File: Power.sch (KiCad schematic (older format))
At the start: 17 parts, among them CON1 PWR_JACK, P1 PWR_USB, U1 MCP16312-E/MS

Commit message: Schematic changes. PCB in process of making.
Removed LAN9500A Jtag. Removed Aria G25 pinout. Removed USB connectors. Added rezistors to USB/ETH/ySD shields.
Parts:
- removed P1: PWR_USB, symbol USB_OTG
- CON1: footprint (none) -> Connectors:BARREL_JACK
- D1, D2: footprint (none) -> Diodes_SMD:D_SMA_Handsoldering
- L1: footprint (none) -> Choke_SMD:Choke_SMD_1206_Handsoldering
- U1: footprint (none) -> Housings_SSOP:MSOP-8-1EP_3x3mm_Pitch0.65mm
- W1: footprint (none) -> Measurement_Points:Measurement_Point_Square-SMD-Pad_Small
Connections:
- net VBUS: now reaches D1.2 (A)
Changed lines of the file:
@@
 F 0 "CON1" H 3600 2850 50  0000 C CNN
 F 1 "PWR_JACK" H 3600 2400 50  0000 C CNN
-F 2 "" H 3600 2600 50  0001 C CNN
+F 2 "Connectors:BARREL_JACK" H 3600 2600 50  0001 C CNN
 F 3 "" H 3600 2600 50  0000 C CNN
 	1    3600 2600
 	1    0    0    -1
-$EndComp
-$Comp
-L USB_OTG P1
-U 1 1 587BE3DA
-P 4250 3700
-F 0 "P1" V 4575 3575 50  0000 C CNN
-F 1 "PWR_USB" V 3950 3700 50  0000 C CNN
-F 2 "" V 4200 3600 50  0001 C CNN
-F 3 "" V 4200 3600 50  0000 C CNN
-	1    4250 3700
-	0    1    1    0
 $EndComp
 $Comp
@@
 $EndComp
 $Comp
-L GND #PWR02
-U 1 1 587BE697
-P 4350 4200
-F 0 "#PWR02" H 4350 3950 50  0001 C CNN
-F 1 "GND" H 4350 4050 50  0000 C CNN
-F 2 "" H 4350 4200 50  0000 C CNN
-F 3 "" H 4350 4200 50  0000 C CNN
-	1    4350 4200
-	1    0    0    -1
-$EndComp
-$Comp
-L GND #PWR03
-U 1 1 587BE6AA
-P 3850 4000
-F 0 "#PWR03" H 3850 3750 50  0001 C CNN
-F 1 "GND" H 3850 3850 50  0000 C CNN
-F 2 "" H 3850 4000 50  0000 C CNN
-F 3 "" H 3850 4000 50  0000 C CNN
-	1    3850 4000
-	1    0    0    -1
-$EndComp
-$Comp
-L PWR_FLAG #FLG04
+L PWR_FLAG #FLG02
 U 1 1 587BE76C
 P 8150 2500
-F 0 "#FLG04" H 8150 2595 50  0001 C CNN
+F 0 "#FLG02" H 8150 2595 50  0001 C CNN
 F 1 "PWR_FLAG" H 8050 2700 50  0000 C CNN
 F 2 "" H 8150 2500 50  0000 C CNN
@@
 F 0 "D2" H 4250 2400 50  0000 C CNN
 F 1 "Schottky" H 4300 2600 50  0000 C CNN
-F 2 "" H 4250 2500 50  0001 C CNN
+F 2 "Diodes_SMD:D_SMA_Handsoldering" H 4250 2500 50  0001 C CNN
 F 3 "" H 4250 2500 50  0000 C CNN
 	1    4250 2500
@@
 F 0 "U1" H 6550 2400 50  0000 C CNN
 F 1 "MCP16312-E/MS" H 6550 2950 50  0000 C CNN
-F 2 "" H 6600 2900 60  0001 C CNN
+F 2 "Housings_SSOP:MSOP-8-1EP_3x3mm_Pitch0.65mm" H 6600 2900 60  0001 C CNN
 F 3 "" H 6600 2900 60  0001 C CNN
 	1    6500 2650
@@
 $EndComp
 $Comp
-L GND #PWR05
+L GND #PWR03
 U 1 1 587BECE9
 P 5950 2900
-F 0 "#PWR05" H 5950 2650 50  0001 C CNN
+F 0 "#PWR03" H 5950 2650 50  0001 C CNN
 F 1 "GND" H 5950 2750 50  0000 C CNN
 F 2 "" H 5950 2900 50  0000 C CNN
@@
 $EndComp
 $Comp
-L GND #PWR06
+L GND #PWR04
 U 1 1 587BED67
 P 5750 3200
-F 0 "#PWR06" H 5750 2950 50  0001 C CNN
+F 0 "#PWR04" H 5750 2950 50  0001 C CNN
 F 1 "GND" H 5750 3050 50  0000 C CNN
 F 2 "" H 5750 3200 50  0000 C CNN
@@
 $EndComp
 $Comp
-L GND #PWR07
+L GND #PWR05
 U 1 1 587BEE32
 P 5550 3000
-F 0 "#PWR07" H 5550 2750 50  0001 C CNN
+F 0 "#PWR05" H 5550 2750 50  0001 C CNN
 F 1 "GND" H 5550 2850 50  0000 C CNN
 F 2 "" H 5550 3000 50  0000 C CNN
@@
 $EndComp
 $Comp
-L GND #PWR08
+L GND #PWR06
 U 1 1 587BEE52
 P 5300 3000
-F 0 "#PWR08" H 5300 2750 50  0001 C CNN
+F 0 "#PWR06" H 5300 2750 50  0001 C CNN
 F 1 "GND" H 5300 2850 50  0000 C CNN
 F 2 "" H 5300 3000 50  0000 C CNN
@@
 VIN
 $Comp
-L GND #PWR09
+L GND #PWR07
 U 1 1 587BF3B1
 P 7100 2900
-F 0 "#PWR09" H 7100 2650 50  0001 C CNN
+F 0 "#PWR07" H 7100 2650 50  0001 C CNN
 F 1 "GND" H 7100 2750 50  0000 C CNN
 F 2 "" H 7100 2900 50  0000 C CNN
@@
 F 0 "L1" V 7600 2700 50  0000 C CNN
 F 1 "15uH" V 7750 2600 50  0000 C CNN
-F 2 "" H 7650 2600 50  0001 C CNN
+F 2 "Choke_SMD:Choke_SMD_1206_Handsoldering" H 7650 2600 50  0001 C CNN
 F 3 "" H 7650 2600 50  0000 C CNN
 	1    7650 2600
@@
 $EndComp
 $Comp
-L GND #PWR010
+L GND #PWR08
 U 1 1 587BF576
 P 7900 3500
-F 0 "#PWR010" H 7900 3250 50  0001 C CNN
+F 0 "#PWR08" H 7900 3250 50  0001 C CNN
 F 1 "GND" H 7900 3350 50  0000 C CNN
 F 2 "" H 7900 3500 50  0000 C CNN
@@
 $EndComp
 $Comp
-L GND #PWR011
+L GND #PWR09
 U 1 1 587BFB09
 P 8150 3100
-F 0 "#PWR011" H 8150 2850 50  0001 C CNN
+F 0 "#PWR09" H 8150 2850 50  0001 C CNN
 F 1 "GND" H 8150 2950 50  0000 C CNN
 F 2 "" H 8150 3100 50  0000 C CNN
@@
 $EndComp
 $Comp
-L GND #PWR012
+L GND #PWR010
 U 1 1 587BFB3B
 P 8400 3100
-F 0 "#PWR012" H 8400 2850 50  0001 C CNN
+F 0 "#PWR010" H 8400 2850 50  0001 C CNN
 F 1 "GND" H 8400 2950 50  0000 C CNN
 F 2 "" H 8400 3100 50  0000 C CNN
@@
 $EndComp
 $Comp
-L +3.3V #PWR013
+L +3.3V #PWR011
 U 1 1 587C072D
 P 8400 2500
-F 0 "#PWR013" H 8400 2350 50  0001 C CNN
+F 0 "#PWR011" H 8400 2350 50  0001 C CNN
 F 1 "+3.3V" H 8400 2640 50  0000 C CNN
 F 2 "" H 8400 2500 50  0000 C CNN
@@
 Wire Wire Line
 	3950 3500 3850 3500
-Wire Wire Line
-	3850 3900 3850 4000
-Wire Wire Line
-	3850 3900 3950 3900
-Wire Wire Line
-	4350 4200 4350 4100
 Wire Wire Line
 	4000 2600 4000 2800
@@
 F 0 "D1" H 3700 3600 50  0000 C CNN
 F 1 "Schottky" H 3700 3400 50  0000 C CNN
-F 2 "" H 3700 3500 50  0001 C CNN
+F 2 "Diodes_SMD:D_SMA_Handsoldering" H 3700 3500 50  0001 C CNN
 F 3 "" H 3700 3500 50  0000 C CNN
 	1    3700 3500
@@
 $EndComp
 $Comp
-L GND #PWR014
+L GND #PWR012
 U 1 1 58981582
 P 8750 3500
-F 0 "#PWR014" H 8750 3250 50  0001 C CNN
+F 0 "#PWR012" H 8750 3250 50  0001 C CNN
 F 1 "GND" H 8750 3350 50  0000 C CNN
 F 2 "" H 8750 3500 50  0000 C CNN
@@
 F 0 "W1" H 8750 2770 50  0000 C CNN
 F 1 "3.3V_T" H 8750 2700 50  0000 C CNN
-F 2 "" H 8950 2500 50  0001 C CNN
+F 2 "Measurement_Points:Measurement_Point_Square-SMD-Pad_Small" H 8950 2500 50  0001 C CNN
 F 3 "" H 8950 2500 50  0000 C CNN
 	1    8750 2500
@@
 $EndComp
 Connection ~ 8750 2600
+Text HLabel 3950 3500 2    50   Input ~ 0
+VBUS
 $EndSCHEMATC

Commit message: Modified USB/ETH label names.
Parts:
- R1, R2, R3: footprint Resistors_SMD:R_0805_HandSoldering -> Resistors_SMD:R_0603_HandSoldering
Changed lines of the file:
@@
 F 0 "R1" V 7980 2850 50  0000 C CNN
 F 1 "31k6" V 7800 2850 50  0000 C CNN
-F 2 "Resistors_SMD:R_0805_HandSoldering" V 7830 2850 50  0001 C CNN
+F 2 "Resistors_SMD:R_0603_HandSoldering" V 7830 2850 50  0001 C CNN
 F 3 "" H 7900 2850 50  0000 C CNN
 	1    7900 2850
@@
 F 0 "R2" V 7980 3250 50  0000 C CNN
 F 1 "10k" V 7800 3250 50  0000 C CNN
-F 2 "Resistors_SMD:R_0805_HandSoldering" V 7830 3250 50  0001 C CNN
+F 2 "Resistors_SMD:R_0603_HandSoldering" V 7830 3250 50  0001 C CNN
 F 3 "" H 7900 3250 50  0000 C CNN
 	1    7900 3250
@@
 F 0 "R3" V 8830 3250 50  0000 C CNN
 F 1 "R" V 8750 3250 50  0000 C CNN
-F 2 "Resistors_SMD:R_0805_HandSoldering" V 8680 3250 50  0001 C CNN
+F 2 "Resistors_SMD:R_0603_HandSoldering" V 8680 3250 50  0001 C CNN
 F 3 "" H 8750 3250 50  0000 C CNN
 	1    8750 3250

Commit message: Finished first version of PCB.
Modified RJ45 footprint.
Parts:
- C1, C2: footprint Capacitors_SMD:C_0805_HandSoldering -> Capacitors_SMD:CP_Elec_5x4.5
- R3: value R -> 220
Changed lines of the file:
@@
 F 0 "C1" H 5200 2850 50  0000 L CNN
 F 1 "10uF" H 5100 2650 50  0000 L CNN
-F 2 "Capacitors_SMD:C_0805_HandSoldering" H 5338 2600 50  0001 C CNN
+F 2 "Capacitors_SMD:CP_Elec_5x4.5" H 5338 2600 50  0001 C CNN
 F 3 "" H 5300 2750 50  0000 C CNN
 	1    5300 2750
@@
 F 0 "C2" H 5450 2850 50  0000 L CNN
 F 1 "10uF" H 5350 2650 50  0000 L CNN
-F 2 "Capacitors_SMD:C_0805_HandSoldering" H 5588 2600 50  0001 C CNN
+F 2 "Capacitors_SMD:CP_Elec_5x4.5" H 5588 2600 50  0001 C CNN
 F 3 "" H 5550 2750 50  0000 C CNN
 	1    5550 2750
@@
 P 8750 3250
 F 0 "R3" V 8830 3250 50  0000 C CNN
-F 1 "R" V 8750 3250 50  0000 C CNN
+F 1 "220" V 8750 3250 50  0000 C CNN
 F 2 "Resistors_SMD:R_0603_HandSoldering" V 8680 3250 50  0001 C CNN
 F 3 "" H 8750 3250 50  0000 C CNN

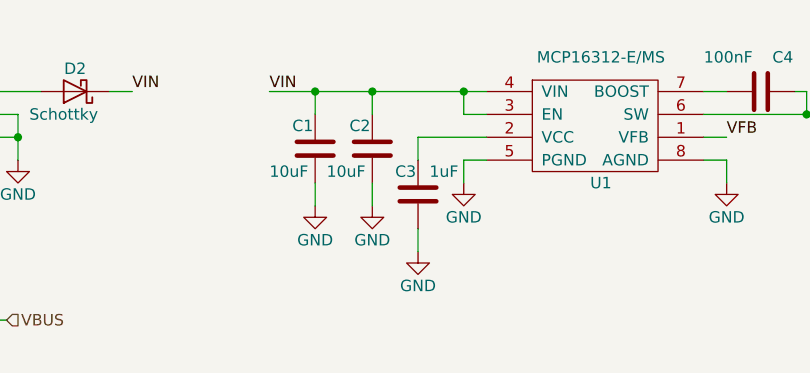
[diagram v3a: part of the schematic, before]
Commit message: Modified buck circuit on board.
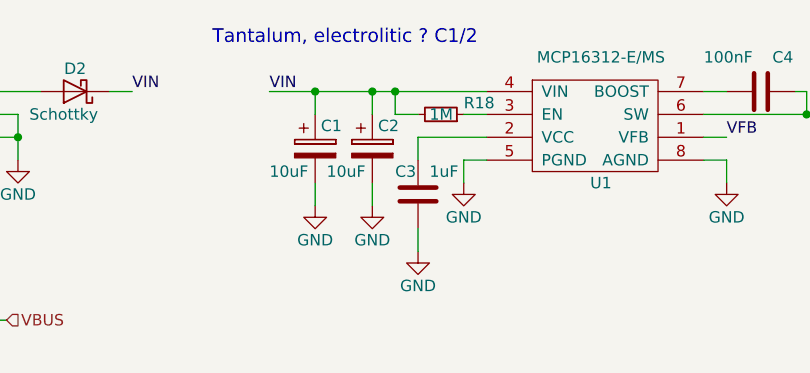
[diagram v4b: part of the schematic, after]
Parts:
- removed C1, C2: 10uF, Capacitors_SMD:CP_Elec_5x4.5, symbol C
- added C1, C2: 10uF, Capacitors_SMD:C_0603_HandSoldering, symbol CP
- added R18: 1M, Resistors_SMD:R_0603_HandSoldering, symbol R_Small
- C3, C4, C5, C6: footprint Capacitors_SMD:C_0805_HandSoldering -> Capacitors_SMD:C_0603_HandSoldering
- D3: footprint LEDs:LED_0805 -> LEDs:LED_0603
- L1: footprint Choke_SMD:Choke_SMD_1206_Handsoldering -> Inductors:Inductor_Taiyo-Yuden_MD-5050
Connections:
- net GND: now also C1.2, C2.2
- net VIN: now also C1.1, C2.1, R18.2; no longer U1.3 (EN)
- new net: R18.1, U1.3 (EN)
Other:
- note added: "Tantalum, electrolitic ? C1/2"
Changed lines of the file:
@@
 F 0 "C3" H 5650 3050 50  0000 L CNN
 F 1 "1uF" H 5800 3050 50  0000 L CNN
-F 2 "Capacitors_SMD:C_0805_HandSoldering" H 5788 2800 50  0001 C CNN
+F 2 "Capacitors_SMD:C_0603_HandSoldering" H 5788 2800 50  0001 C CNN
 F 3 "" H 5750 2950 50  0000 C CNN
 	1    5750 2950
-	1    0    0    -1
-$EndComp
-$Comp
-L C C1
-U 1 1 587BEC9F
-P 5300 2750
-F 0 "C1" H 5200 2850 50  0000 L CNN
-F 1 "10uF" H 5100 2650 50  0000 L CNN
-F 2 "Capacitors_SMD:CP_Elec_5x4.5" H 5338 2600 50  0001 C CNN
-F 3 "" H 5300 2750 50  0000 C CNN
-	1    5300 2750
 	1    0    0    -1
 $EndComp
@@
 $EndComp
 $Comp
-L C C2
-U 1 1 587BEDBB
-P 5550 2750
-F 0 "C2" H 5450 2850 50  0000 L CNN
-F 1 "10uF" H 5350 2650 50  0000 L CNN
-F 2 "Capacitors_SMD:CP_Elec_5x4.5" H 5588 2600 50  0001 C CNN
-F 3 "" H 5550 2750 50  0000 C CNN
-	1    5550 2750
-	1    0    0    -1
-$EndComp
-$Comp
 L GND #PWR05
 U 1 1 587BEE32
@@
 F 0 "L1" V 7600 2700 50  0000 C CNN
 F 1 "15uH" V 7750 2600 50  0000 C CNN
-F 2 "Choke_SMD:Choke_SMD_1206_Handsoldering" H 7650 2600 50  0001 C CNN
+F 2 "Inductors:Inductor_Taiyo-Yuden_MD-5050" H 7650 2600 50  0001 C CNN
 F 3 "" H 7650 2600 50  0000 C CNN
 	1    7650 2600
@@
 F 0 "C4" V 7100 2550 50  0000 L CNN
 F 1 "100nF" V 7100 2250 50  0000 L CNN
-F 2 "Capacitors_SMD:C_0805_HandSoldering" H 7288 2350 50  0001 C CNN
+F 2 "Capacitors_SMD:C_0603_HandSoldering" H 7288 2350 50  0001 C CNN
 F 3 "" H 7250 2500 50  0000 C CNN
 	1    7250 2500
@@
 F 0 "C5" H 8175 2950 50  0000 L CNN
 F 1 "10uF" H 8175 2750 50  0000 L CNN
-F 2 "Capacitors_SMD:C_0805_HandSoldering" H 8188 2700 50  0001 C CNN
+F 2 "Capacitors_SMD:C_0603_HandSoldering" H 8188 2700 50  0001 C CNN
 F 3 "" H 8150 2850 50  0000 C CNN
 	1    8150 2850
@@
 F 0 "C6" H 8425 2950 50  0000 L CNN
 F 1 "10uF" H 8425 2750 50  0000 L CNN
-F 2 "Capacitors_SMD:C_0805_HandSoldering" H 8438 2700 50  0001 C CNN
+F 2 "Capacitors_SMD:C_0603_HandSoldering" H 8438 2700 50  0001 C CNN
 F 3 "" H 8400 2850 50  0000 C CNN
 	1    8400 2850
@@
 	6050 2600 5950 2600
 Wire Wire Line
-	5950 2600 5950 2500
-Wire Wire Line
-	5100 2500 6050 2500
-Wire Wire Line
 	5950 2900 5950 2800
 Wire Wire Line
@@
 Wire Wire Line
 	5550 2500 5550 2600
-Connection ~ 5950 2500
 Wire Wire Line
 	5300 2500 5300 2600
@@
 F 0 "D3" H 8750 2950 50  0000 C CNN
 F 1 "PWR_LED" H 8750 2750 50  0000 C CNN
-F 2 "LEDs:LED_0805" H 8750 2850 50  0001 C CNN
+F 2 "LEDs:LED_0603" H 8750 2850 50  0001 C CNN
 F 3 "" H 8750 2850 50  0000 C CNN
 	1    8750 2850
@@
 Text HLabel 3950 3500 2    50   Input ~ 0
 VBUS
+$Comp
+L CP C1
+U 1 1 58B7F09F
+P 5300 2750
+F 0 "C1" H 5325 2850 50  0000 L CNN
+F 1 "10uF" H 5100 2650 50  0000 L CNN
+F 2 "Capacitors_SMD:C_0603_HandSoldering" H 5338 2600 50  0001 C CNN
+F 3 "" H 5300 2750 50  0000 C CNN
+	1    5300 2750
+	1    0    0    -1
+$EndComp
+$Comp
+L CP C2
+U 1 1 58B7F361
+P 5550 2750
+F 0 "C2" H 5575 2850 50  0000 L CNN
+F 1 "10uF" H 5350 2650 50  0000 L CNN
+F 2 "Capacitors_SMD:C_0603_HandSoldering" H 5588 2600 50  0001 C CNN
+F 3 "" H 5550 2750 50  0000 C CNN
+	1    5550 2750
+	1    0    0    -1
+$EndComp
+Text Notes 4850 2300 0    60   ~ 0
+Tantalum, electrolitic ? C1/2
+$Comp
+L R_Small R18
+U 1 1 58B7E269
+P 5850 2600
+F 0 "R18" V 5900 2700 50  0000 L CNN
+F 1 "1M" V 5850 2550 50  0000 L CNN
+F 2 "Resistors_SMD:R_0603_HandSoldering" H 5850 2600 50  0001 C CNN
+F 3 "" H 5850 2600 50  0000 C CNN
+	1    5850 2600
+	0    1    -1   0
+$EndComp
+Wire Wire Line
+	5750 2600 5650 2600
+Wire Wire Line
+	5650 2600 5650 2500
+Connection ~ 5650 2500
+Wire Wire Line
+	5100 2500 6050 2500
 $EndSCHEMATC

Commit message: Modified schematic. v1.1
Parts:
- added C1, C2, C4, C6: 10uF, Capacitors_Tantalum_SMD:CP_Tantalum_Case-C_EIA-6032-28_Hand, symbol CP
- added C10: 100nF, Capacitors_SMD:C_0603_HandSoldering, symbol C
- added C12, C14: 10uF, Capacitors_SMD:C_0603_HandSoldering, symbol C
- added C8: 1uF, Capacitors_SMD:C_0603_HandSoldering, symbol C
- added D4: PWR_LED, LEDs:LED_0603, symbol LED
- added L2: 22uH, Inductors:Inductor_Taiyo-Yuden_MD-5050, symbol L
- added R2: 1M, Resistors_SMD:R_0603_HandSoldering, symbol R_Small
- added R5: 52k3, Resistors_SMD:R_0603_HandSoldering, symbol R
- added R6: 10k, Resistors_SMD:R_0603_HandSoldering, symbol R
- added R8: 220, Resistors_SMD:R_0603_HandSoldering, symbol R
- added U2: MCP16312-E/MS, Housings_SSOP:MSOP-8_3x3mm_Pitch0.65mm, symbol MCP16312-E/MS
- added W1: VBUS_T, Measurement_Points:Measurement_Point_Round-SMD-Pad_Small, symbol TEST_1P
- added W2: VIN_T, Measurement_Points:Measurement_Point_Round-SMD-Pad_Small, symbol TEST_1P
- added W4: 5V_T, Measurement_Points:Measurement_Point_Round-SMD-Pad_Small, symbol TEST_1P
- C3: renamed from C1; footprint Capacitors_SMD:C_0603_HandSoldering -> Capacitors_Tantalum_SMD:CP_Tantalum_Case-C_EIA-6032-28_Hand
- C5: renamed from C2; footprint Capacitors_SMD:C_0603_HandSoldering -> Capacitors_Tantalum_SMD:CP_Tantalum_Case-C_EIA-6032-28_Hand
- D1, D2: footprint Diodes_SMD:D_SMA_Handsoldering -> Diodes_SMD:D_SMA-SMB_Universal_Handsoldering
- U1: footprint Housings_SSOP:MSOP-8-1EP_3x3mm_Pitch0.65mm -> Housings_SSOP:MSOP-8_3x3mm_Pitch0.65mm
- W3: renamed from W1; footprint Measurement_Points:Measurement_Point_Square-SMD-Pad_Small -> Measurement_Points:Measurement_Point_Round-SMD-Pad_Small
- renumbered C5 to C11, C6 to C13, C3 to C7, C4 to C9, R18 to R1, R1 to R3, R2 to R4, R3 to R7
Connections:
- net GND: now also C1.2, C12.2, C14.2, C2.2, C4.2, C6.2, C8.2, R6.2, R8.1, U2.5 (PGND), U2.8 (AGND)
- net VIN: now also C1.1, C2.1, C4.1, C6.1, R2.2, U2.4 (VIN), W1.1, W2.1
- net VFB renamed 3V3_VFB
- new net: C8.1, U2.2 (VCC)
- new net: R2.1, U2.3 (EN)
- new net: C10.1, L2.2, U2.6 (SW)
- new net: C10.2, U2.7 (BOOST)
- new net: D4.1 (K), R8.2
- new net +5V: C12.1, C14.1, D4.2 (A), L2.1, R5.1, W4.1
- new net 5V_VFB: R5.2, R6.1, U2.1 (VFB)
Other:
- note removed: "Tantalum, electrolitic ? C1/2"
- moved on the sheet: C11, C13, C3, C5, C7, C9, CON1, D1, D2, D3, L1, R1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

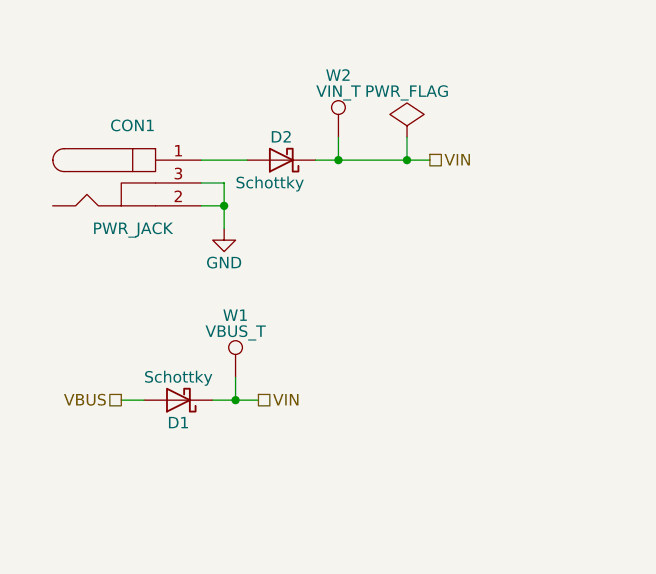
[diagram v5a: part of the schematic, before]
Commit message: Modified board. v1.1 to reflect the schematic change.
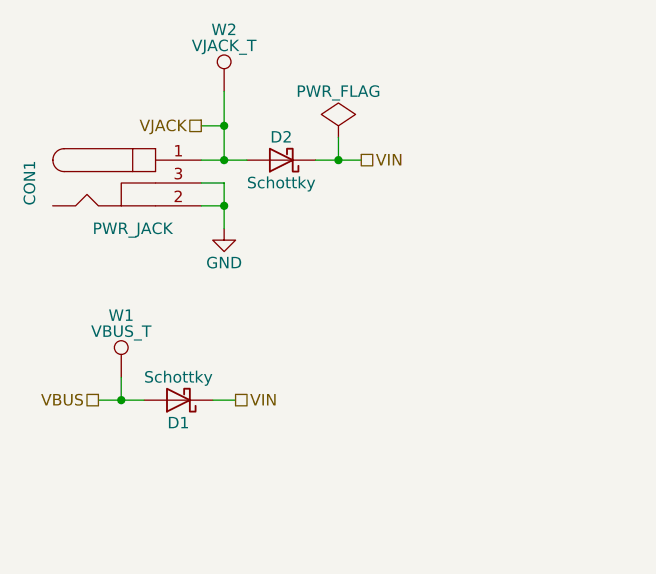
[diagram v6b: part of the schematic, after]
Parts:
- C1, C2, C3, C4, C5, C6: footprint Capacitors_Tantalum_SMD:CP_Tantalum_Case-C_EIA-6032-28_Hand -> Capacitors_Tantalum_SMD:CP_Tantalum_Case-B_EIA-3528-21_Hand
- W2: value VIN_T -> VJACK_T
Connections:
- net VBUS: now also W1.1
- net VIN: no longer W1.1, W2.1
- net VJACK: now reaches CON1.1, D2.2 (A)
- net VJACK: now also W2.1
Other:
- moved on the sheet: W1, W2
